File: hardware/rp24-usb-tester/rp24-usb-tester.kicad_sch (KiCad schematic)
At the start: 40 parts, among them J1 SPEAKER, J2 POWER, J3 EXT_CAP, J4 505070-2422, J5 RAILS, J6 AUX, J7 MOTOR, P1 USB_C_Receptacle_USB2.0_16P, Q1 SS8050, Q2 SS8050, Q3 SS8050, Q4 SS8050, Q5 SS8050, U1 MT2492

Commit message: chore: update e24 connector model
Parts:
- J4: footprint 5050702422 -> rp24-usb-tester:CONN-SMD_24P-P0.35_5050702422
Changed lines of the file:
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@@
 			)
 		)
-		(property "Footprint" "5050702422"
+		(property "Footprint" "rp24-usb-tester:CONN-SMD_24P-P0.35_5050702422"
 			(at 243.84 76.2 0)
 			(effects

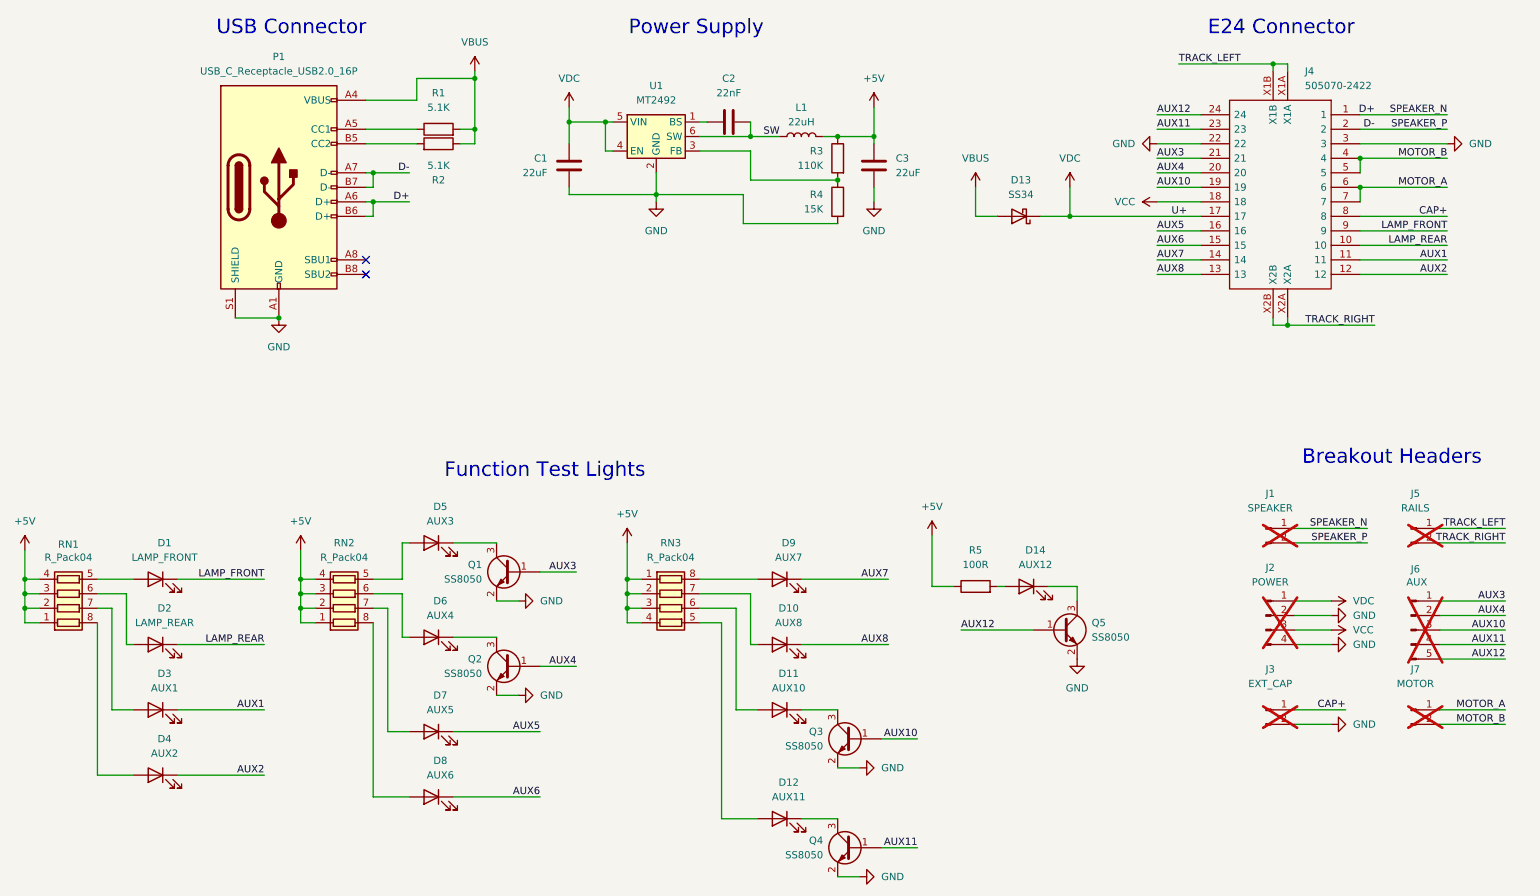
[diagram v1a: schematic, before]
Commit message: feat: move usb to aux11/aux12 pins
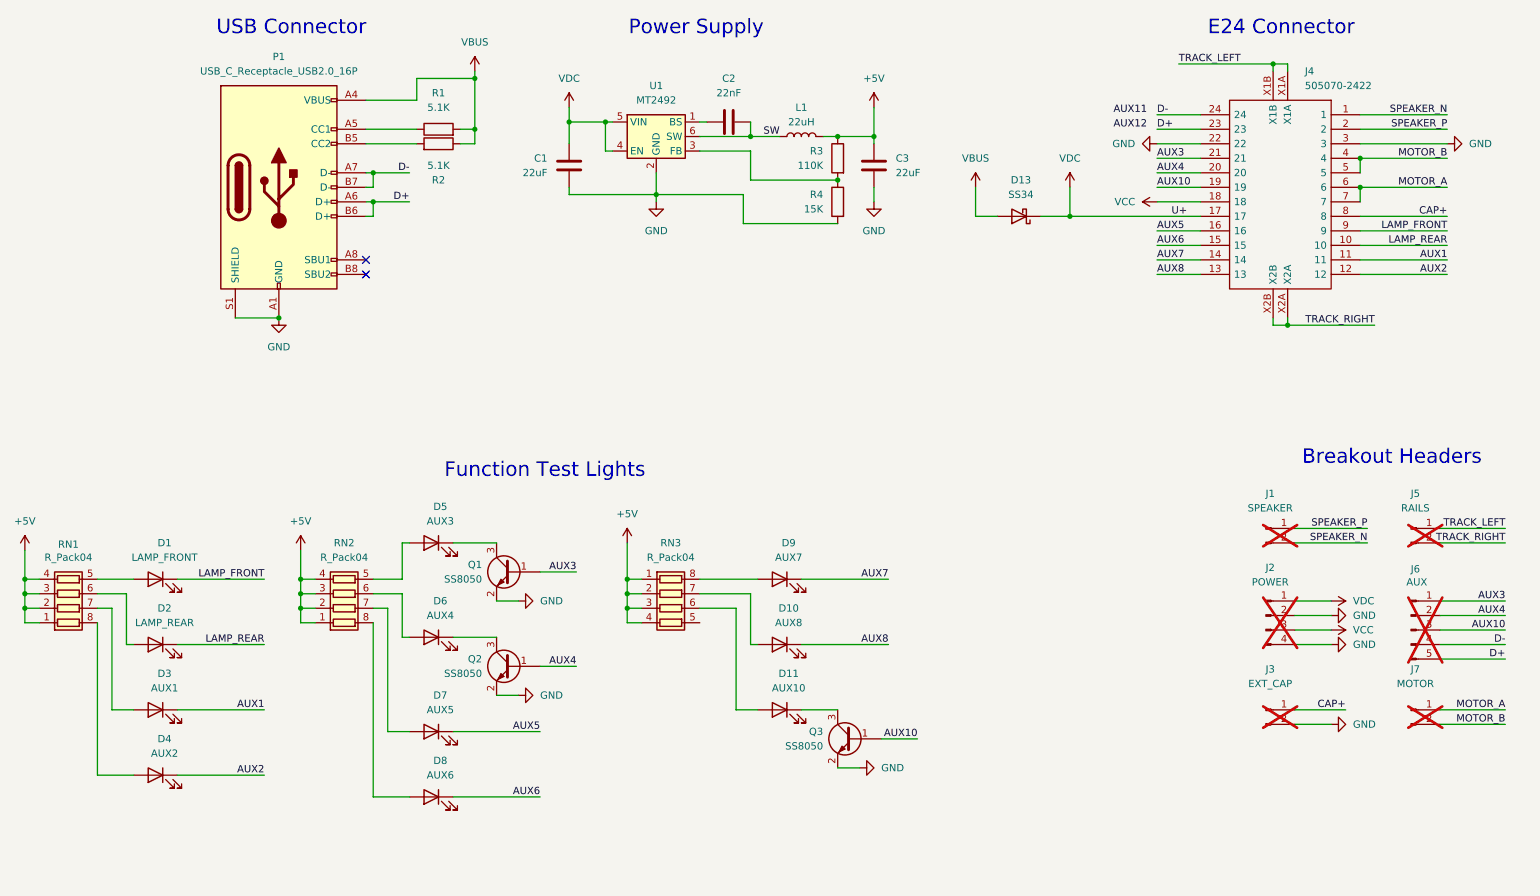
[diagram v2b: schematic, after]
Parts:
- removed D12: AUX11, LED_SMD:LED_0603_1608Metric, symbol rp24-usb-tester:LED
- removed D14: AUX12, LED_SMD:LED_0603_1608Metric, symbol rp24-usb-tester:LED
- removed Q4, Q5: SS8050, Package_TO_SOT_SMD:SOT-23, symbol rp24-usb-tester:SS8050
- removed R5: 100R, Resistor_SMD:R_0402_1005Metric, symbol rp24-usb-tester:R
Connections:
- net AUX11: no longer J4.23, J6.4 (Pin_4)
- net AUX12: no longer J4.24, J6.5 (Pin_5)
- net D+: now also J4.23, J6.5 (Pin_5); no longer J1.1 (Pin_1), J4.1
- net D-: now also J4.24, J6.4 (Pin_4); no longer J1.2 (Pin_2), J4.2
- new net SPEAKER_N: J1.2 (Pin_2), J4.1
- new net SPEAKER_P: J1.1 (Pin_1), J4.2
